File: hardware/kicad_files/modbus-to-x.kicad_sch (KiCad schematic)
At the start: 63 parts, among them J1 PWR, J2 UART, J3 Screw_Terminal_3.5mm_2, J4 SSQ-110-X-X-D, SW1 1825910-7, SW2 1825910-7, U1 AMS1117-3.3, U2 ESP32-WROOM-32DM113DH6400PH3Q0, U3 MAX3485, U5 AT24CS64-XHM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

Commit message: updated datasheets
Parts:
- C22: FriendlyName Cout47uf -> Cin_MAX3485
- J4: PartNo (none) -> SSQ-110-23-L-D
- R1: PartNo RND 1551206S4F1000T5E -> RC1206FR-13120RL
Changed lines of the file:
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@@
 			)
 		)
-		(property "Datasheet" "ESP32-WROOM-32DM113DH6400PH3Q0"
+		(property "Datasheet" "https://www.espressif.com/sites/default/files/documentation/esp32-wroom-32d_esp32-wroom-32u_datasheet_en.pdf"
 			(at 218.948 23.622 0)
 			(effects
@@
 			)
 		)
-		(property "Datasheet" ""
+		(property "Datasheet" "https://docs.rs-online.com/acc8/0900766b8140488f.pdf"
 			(at 245.11 138.43 0)
 			(effects
@@
 			)
 		)
+		(property "PartNo" "SSQ-110-23-L-D"
+			(at 245.11 138.43 90)
+			(effects
+				(font
+					(size 1.27 1.27)
+				)
+				(hide yes)
+			)
+		)
 		(pin "11"
 		)
@@
 			)
 		)
-		(property "FriendlyName" "Cout47uf"
+		(property "FriendlyName" "Cin_MAX3485"
 			(at 36.83 81.28 0)
 			(effects
@@
 			)
 		)
-		(property "Datasheet" "https://media.distrelec.com/Web/Downloads/_t/ds/rnd_smd_resistors_eng_tds.pdf"
+		(property "Datasheet" "https://www.yageo.com/upload/media/product/products/datasheet/rchip/PYu-RC_Group_51_RoHS_L_12.pdf"
 			(at 55.88 99.06 0)
 			(effects
@@
 			)
 		)
-		(property "Description" "Resistor Thick film  100 Ohm     ±1%     SMD 1206 1/4W"
+		(property "Description" "120 Ohms ±1% 0.25W, 1/4W Chip Resistor 1206 (3216 Metric) Moisture Resistant Thick Film"
 			(at 55.88 99.06 0)
 			(effects
@@
 			)
 		)
-		(property "PartNo" "RND 1551206S4F1000T5E"
+		(property "PartNo" "RC1206FR-13120RL"
 			(at 55.88 99.06 90)
 			(effects
 				(font
-					(size 1.27 1.27)
-				)
-				(hide yes)
-			)
-		)
-		(property "ProductCode" ""
-			(at 55.88 99.06 0)
-			(effects
-				(font

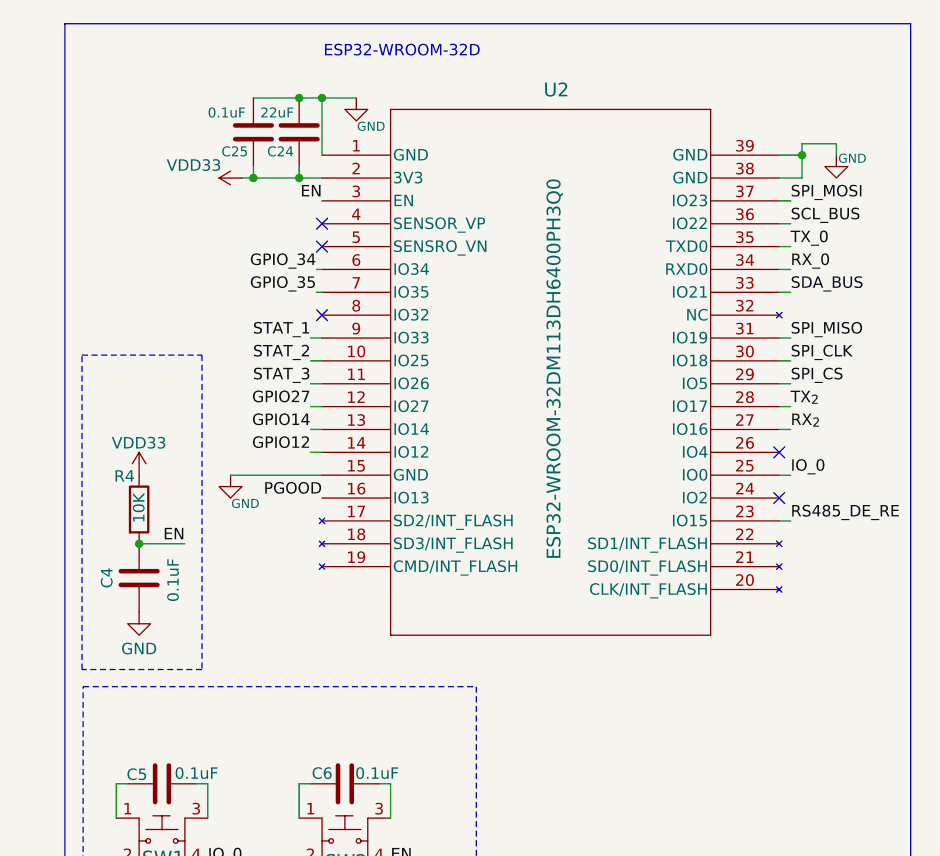
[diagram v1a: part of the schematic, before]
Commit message: fixed esp32 footprint
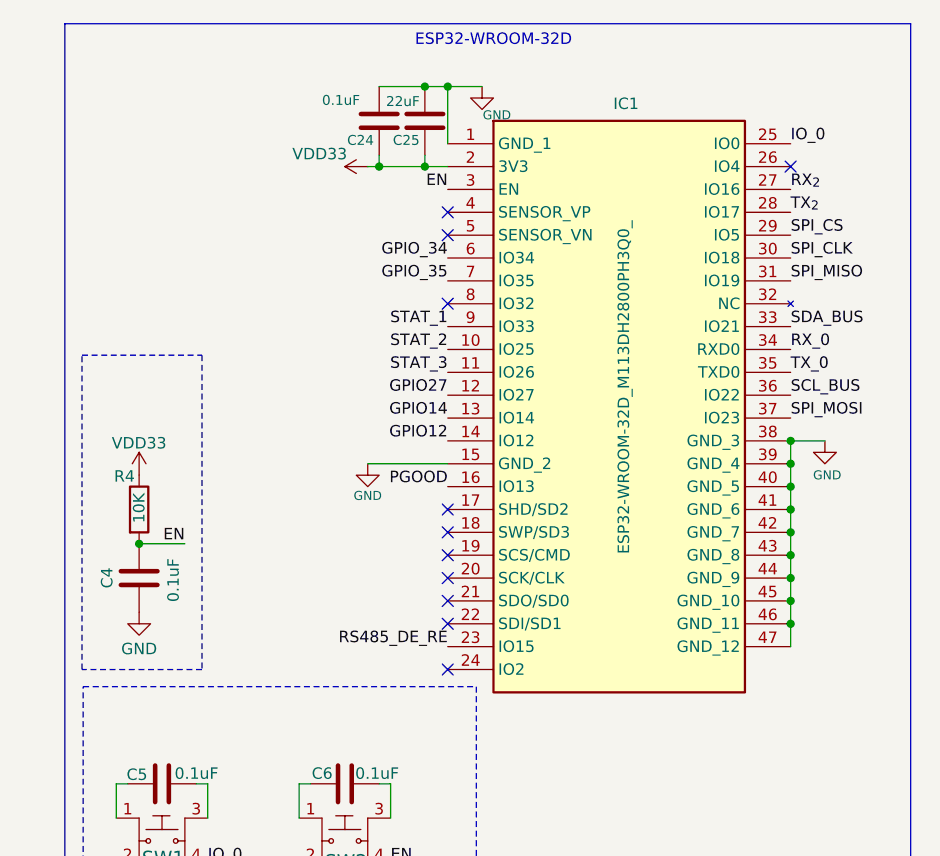
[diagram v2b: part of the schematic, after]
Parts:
- removed U2: ESP32-WROOM-32DM113DH6400PH3Q0, ESP32-WROOM-32D-M113DH6400PH3Q0:ESP32-WROOM-32DM113DH6400PH3Q0_WITH_VIAS, symbol ESP32-WROOM-32D-M113DH6400PH3Q0:ESP32-WROOM-32DM113DH6400PH3Q0
- added IC1: ESP32-WROOM-32D_M113DH2800PH3Q0_, footprint_lib:ESP32-WROOM-32D_M113DH2800PH3Q0, symbol Library:ESP32-WROOM-32D_M113DH2800PH3Q0_
- C24: value 22uF -> 0.1uF; footprint Capacitor_SMD:C_0805_2012Metric_Pad1.18x1.45mm_HandSolder -> Capacitor_SMD:C_1206_3216Metric_Pad1.33x1.80mm_HandSolder; PartNo CL21A226MOCLRNC -> CVNF100K12X; Voltage 16V -> 50V
- C25: value 0.1uF -> 22uF; footprint Capacitor_SMD:C_1206_3216Metric_Pad1.33x1.80mm_HandSolder -> Capacitor_SMD:C_0805_2012Metric_Pad1.18x1.45mm_HandSolder; PartNo CVNF100K12X -> CL21A226MOCLRNC; Voltage 50V -> 16V
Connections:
- net EN: now also IC1.3 (EN)
- net GND: now also IC1.1 (GND_1), IC1.15 (GND_2), IC1.38 (GND_3), IC1.39 (GND_4), IC1.40 (GND_5), IC1.41 (GND_6), IC1.42 (GND_7), IC1.43 (GND_8), IC1.44 (GND_9), IC1.45 (GND_10), IC1.46 (GND_11), IC1.47 (GND_12)
- net GPIO12: now also IC1.14 (IO12)
- net GPIO14: now also IC1.13 (IO14)
- net GPIO27: now also IC1.12 (IO27)
- net GPIO_34: now also IC1.6 (IO34)
- net GPIO_35: now also IC1.7 (IO35)
- net IO_0: now also IC1.25 (IO0)
- net PGOOD: now also IC1.16 (IO13)
- net RS485_DE_RE: now also IC1.23 (IO15)
- net RX_0: now also IC1.34 (RXD0)
- net RX_{2}: now also IC1.27 (IO16)
- net SCL_BUS: now also IC1.36 (IO22)
- net SDA_BUS: now also IC1.33 (IO21)
- net SPI_CLK: now also IC1.30 (IO18)
- net SPI_CS: now also IC1.29 (IO5)
- net SPI_MISO: now also IC1.31 (IO19)
- net SPI_MOSI: now also IC1.37 (IO23)
- net STAT_1: now also IC1.9 (IO33)
- net STAT_2: now also IC1.10 (IO25)
- net STAT_3: now also IC1.11 (IO26)
- net TX_0: now also IC1.35 (TXD0)
- net TX_{2}: now also IC1.28 (IO17)
- net VDD33: now also IC1.2 (3V3)
- no-connect marks 11 -> 17

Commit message: small trace improvements using new ESP footprint
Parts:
- C22: PartNo CHS0001/50 -> NACE1R0M50V4X5.5TR15F
- C23, C24, C4, C5, C6, C9: PartNo CVNF100K12X -> C1206C104K5RACTU
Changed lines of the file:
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@@
 			)
 		)
-		(property "Datasheet" "https://elektronik-lavpris.dk/files/sup2/C1206C104K5RACTU.pdf"
+		(property "Datasheet" "https://content.kemet.com/datasheets/KEM_C1002_X7R_SMD.pdf"
 			(at 224.79 24.13 0)
 			(effects
@@
 			)
 		)
-		(property "Description" "SMD MLC Capacitor 100nF 50V 10% X7R 1206"
+		(property "Description" "0.1 µF ±10% 50V Ceramic Capacitor X7R 1206 (3216 Metric)"
 			(at 224.79 24.13 0)
 			(effects
@@
 			)
 		)
-		(property "PartNo" "CVNF100K12X"
+		(property "PartNo" "C1206C104K5RACTU"
 			(at 224.79 24.13 0)
 			(effects
@@
 			)
 		)
-		(property "Datasheet" "https://elektronik-lavpris.dk/files/sup2/C1206C104K5RACTU.pdf"
+		(property "Datasheet" "https://content.kemet.com/datasheets/KEM_C1002_X7R_SMD.pdf"
 			(at 68.58 138.43 0)
 			(effects
@@
 			)
 		)
-		(property "Description" "SMD MLC Capacitor 100nF 50V 10% X7R 1206"
+		(property "Description" "0.1 µF ±10% 50V Ceramic Capacitor X7R 1206 (3216 Metric)"
 			(at 68.58 138.43 0)
 			(effects
@@
 			)
 		)
-		(property "PartNo" "CVNF100K12X"
+		(property "PartNo" "C1206C104K5RACTU"
 			(at 68.58 138.43 0)
 			(effects
@@
 			)
 		)
-		(property "Datasheet" "https://elektronik-lavpris.dk/files/sup2/C1206C104K5RACTU.pdf"
+		(property "Datasheet" "https://content.kemet.com/datasheets/KEM_C1002_X7R_SMD.pdf"
 			(at 198.12 74.93 0)
 			(effects
@@
 			)
 		)
-		(property "Description" "SMD MLC Capacitor 100nF 50V 10% X7R 1206"
+		(property "Description" "0.1 µF ±10% 50V Ceramic Capacitor X7R 1206 (3216 Metric)"
 			(at 198.12 74.93 0)
 			(effects
@@
 			)
 		)
-		(property "PartNo" "CVNF100K12X"
+		(property "PartNo" "C1206C104K5RACTU"
 			(at 198.12 74.93 0)
 			(effects
@@
 			)
 		)
-		(property "Datasheet" "https://elektronik-lavpris.dk/files/sup2/C1206C104K5RACTU.pdf"
+		(property "Datasheet" "https://content.kemet.com/datasheets/KEM_C1002_X7R_SMD.pdf"
 			(at 26.67 137.16 0)
 			(effects
@@
 			)
 		)
-		(property "Description" "SMD MLC Capacitor 100nF 50V 10% X7R 1206"
+		(property "Description" "0.1 µF ±10% 50V Ceramic Capacitor X7R 1206 (3216 Metric)"
 			(at 26.67 137.16 0)
 			(effects
@@
 			)
 		)
-		(property "PartNo" "CVNF100K12X"
+		(property "PartNo" "C1206C104K5RACTU"
 			(at 26.67 137.16 0)
 			(effects
@@
 			)
 		)
-		(property "Datasheet" "https://elektronik-lavpris.dk/files/sup2/KJ-HT.pdf"
+		(property "Datasheet" "https://www.niccomp.com/wp-content/uploads/catalog/nace.pdf"
 			(at 36.83 81.28 0)
 			(effects
@@
 			)
 		)
-		(property "Description" "SMD El-Capacitor 1uF/50V 4x5,4mm"
+		(property "Description" "1 µF 50 V Aluminum Electrolytic Capacitors Radial, Can - SMD 19.9 Ohm 2000 Hrs @ 85°C"
 			(at 36.83 81.28 0)
 			(effects
@@
 			)
 		)
-		(property "PartNo" "CHS0001/50"
+		(property "PartNo" "NACE1R0M50V4X5.5TR15F"
 			(at 36.83 81.28 0)
 			(effects
@@
 			)
 		)
-		(property "Datasheet" "https://elektronik-lavpris.dk/files/sup2/C1206C104K5RACTU.pdf"
+		(property "Datasheet" "https://content.kemet.com/datasheets/KEM_C1002_X7R_SMD.pdf"
 			(at 220.98 97.79 0)
 			(effects
@@
 			)
 		)
-		(property "Description" "SMD MLC Capacitor 100nF 50V 10% X7R 1206"
+		(property "Description" "0.1 µF ±10% 50V Ceramic Capacitor X7R 1206 (3216 Metric)"
 			(at 220.98 97.79 0)
 			(effects
@@
 			)
 		)
-		(property "PartNo" "CVNF100K12X"
+		(property "PartNo" "C1206C104K5RACTU"
 			(at 220.98 97.79 0)
 			(effects
@@
 			)
 		)
-		(property "Datasheet" "https://elektronik-lavpris.dk/files/sup2/C1206C104K5RACTU.pdf"
+		(property "Datasheet" "https://content.kemet.com/datasheets/KEM_C1002_X7R_SMD.pdf"
 			(at 200.66 97.79 0)
 			(effects
@@
 			)
 		)
-		(property "Description" "SMD MLC Capacitor 100nF 50V 10% X7R 1206"
+		(property "Description" "0.1 µF ±10% 50V Ceramic Capacitor X7R 1206 (3216 Metric)"
 			(at 200.66 97.79 0)
 			(effects
@@
 			)
 		)
-		(property "PartNo" "CVNF100K12X"
+		(property "PartNo" "C1206C104K5RACTU"
 			(at 200.66 97.79 0)
 			(effects

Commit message: added missing component 3dmodels
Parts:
- C1: PartNo CSMK047/35 -> EEH-ZA1V470P
- SW1: Category Switches -> (none); DK_Datasheet_Link https://www.te.com/commerce/DocumentDelivery/DDEController?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 -> (none); DK_Detail_Page /product-detail/en/te-connectivity-alcoswitch-switches/1825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 -> (none); Description_1 SWITCH TACTILE SPST-NO 0.05A 24V -> (none); Digi-Key_PN 450-1804-ND -> (none); Family Tactile Switches -> (none); MPN 1825910-7 -> (none); Manufacturer TE Connectivity ALCOSWITCH Switches -> (none); PartNo (none) -> PTS645SK43SMTR92; Status Active -> (none)
- SW2: Category Switches -> (none); DK_Datasheet_Link https://www.te.com/commerce/DocumentDelivery/DDEController?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 -> (none); DK_Detail_Page /product-detail/en/te-connectivity-alcoswitch-switches/1825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 -> (none); Description_1 SWITCH TACTILE SPST-NO 0.05A 24V -> (none); Digi-Key_PN 450-1804-ND -> (none); Family Tactile Switches -> (none); MPN 1825910-7 -> (none); Manufacturer TE Connectivity ALCOSWITCH Switches -> (none); PartNo (none) -> PTS645SK43SMTR92 LFS; Status Active -> (none)
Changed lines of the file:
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@@
 			)
 		)
-		(property "Datasheet" "https://www.te.com/commerce/DocumentDelivery/DDEController?Action=srchrtrv&DocNm=1825910&DocType=Customer+Drawing&DocLang=English"
+		(property "Datasheet" "https://www.ckswitches.com/media/1471/pts645.pdf"
 			(at 205.74 96.52 0)
 			(effects
@@
 			)
 		)
-		(property "Description" "SWITCH TACTILE SPST-NO 0.05A 24V"
+		(property "Description" "Tactile Switch SPST-NO Top Actuated Surface Mount"
 			(at 200.66 104.14 0)
 			(effects
@@
 			)
 		)
-		(property "Digi-Key_PN" "450-1804-ND"
-			(at 205.74 93.98 0)
-			(effects
-				(font
-					(size 1.524 1.524)
-				)
-				(justify left)
-				(hide yes)
-			)
-		)
-		(property "MPN" "1825910-7"
-			(at 205.74 91.44 0)
-			(effects
-				(font
-					(size 1.524 1.524)
-				)
-				(justify left)
-				(hide yes)
-			)
-		)
-		(property "Category" "Switches"
-			(at 205.74 88.9 0)
-			(effects
-				(font
-					(size 1.524 1.524)
-				)
-				(justify left)
-				(hide yes)
-			)
-		)
-		(property "Family" "Tactile Switches"
-			(at 205.74 86.36 0)
-			(effects
-				(font
-					(size 1.524 1.524)
-				)
-				(justify left)
-				(hide yes)
-			)
-		)
-		(property "DK_Datasheet_Link" "https://www.te.com/commerce/DocumentDelivery/DDEController?Action=srchrtrv&DocNm=1825910&DocType=Customer+Drawing&DocLang=English"
-			(at 205.74 83.82 0)
-			(effects
-				(font
-					(size 1.524 1.524)
-				)
-				(justify left)
-				(hide yes)
-			)
-		)
-		(property "DK_Detail_Page" "/product-detail/en/te-connectivity-alcoswitch-switches/1825910-7/450-1804-ND/1731414"
-			(at 205.74 81.28 0)
-			(effects
-				(font
-					(size 1.524 1.524)
-				)
-				(justify left)
-				(hide yes)
-			)
-		)
-		(property "Description_1" "SWITCH TACTILE SPST-NO 0.05A 24V"
-			(at 205.74 78.74 0)
-			(effects
-				(font
-					(size 1.524 1.524)
-				)
-				(justify left)
-				(hide yes)
-			)
-		)
-		(property "Manufacturer" "TE Connectivity ALCOSWITCH Switches"
-			(at 205.74 76.2 0)
-			(effects
-				(font
-					(size 1.524 1.524)
-				)
-				(justify left)
-				(hide yes)
-			)
-		)
-		(property "Status" "Active"
-			(at 205.74 73.66 0)
+		(property "PartNo" "PTS645SK43SMTR92"
+			(at 200.66 104.14 0)
 			(effects
 				(font
-					(size 1.524 1.524)
+					(size 1.27 1.27)
 				)
-				(justify left)
 				(hide yes)
 			)
@@
 			)
 		)
-		(property "Datasheet" "LMR14020SQDPRTQ1"
+		(property "Datasheet" "LMR14020QDPRRQ1"
 			(at 76.2 40.64 0)
 			(effects
@@
 			)
 		)
-		(property "Description" "SIMPLE SWITCHER® Power Converter 40V 2A, 2.2MHz Step-Down Converter With 40µA IQ"
+		(property "Description" "Buck Switching Regulator IC Positive Adjustable 0.8V 1 Output 2A 10-WDFN Exposed Pad"
 			(at 76.2 40.64 0)
 			(effects
@@
 			)
 		)
-		(property "Datasheet" "https://elektronik-lavpris.dk/files/sup2/CSM.pdf"
+		(property "Datasheet" "https://industrial.panasonic.com/cdbs/www-data/pdf/RDD0000/ABA0000C1221.pdf"
 			(at 31.75 31.75 0)
 			(effects
@@
 			)
 		)
-		(property "Description" "SMD El-Capacitor 47uF/35V 6,3x5,4mm"
+		(property "Description" "47 µF 35 V Aluminum - Polymer Capacitors Radial, Can - SMD 60mOhm 10000 Hrs @ 105°C"
 			(at 31.75 31.75 0)
 			(effects
@@
 			)
 		)
-		(property "PartNo" "CSMK047/35"
+		(property "PartNo" "EEH-ZA1V470P"
 			(at 31.75 31.75 0)
 			(effects
@@
 			)
 		)
-		(property "Datasheet" "https://www.te.com/commerce/DocumentDelivery/DDEController?Action=srchrtrv&DocNm=1825910&DocType=Customer+Drawing&DocLang=English"
+		(property "Datasheet" "https://www.ckswitches.com/media/1471/pts645.pdf"
 			(at 226.06 96.52 0)
 			(effects
@@
 			)
 		)
-		(property "Description" "SWITCH TACTILE SPST-NO 0.05A 24V"
+		(property "Description" "Tactile Switch SPST-NO Top Actuated Surface Mount"
 			(at 220.98 104.14 0)
 			(effects
@@
 			)
 		)
-		(property "Digi-Key_PN" "450-1804-ND"
-			(at 226.06 93.98 0)
-			(effects
-				(font
-					(size 1.524 1.524)
-				)
-				(justify left)
-				(hide yes)
-			)
-		)
-		(property "MPN" "1825910-7"
-			(at 226.06 91.44 0)
-			(effects
-				(font
-					(size 1.524 1.524)
-				)
-				(justify left)
-				(hide yes)
-			)
-		)
-		(property "Category" "Switches"
-			(at 226.06 88.9 0)
-			(effects
-				(font
-					(size 1.524 1.524)
-				)
-				(justify left)
-				(hide yes)
-			)
-		)
-		(property "Family" "Tactile Switches"
-			(at 226.06 86.36 0)
-			(effects
-				(font
-					(size 1.524 1.524)
-				)
-				(justify left)
-				(hide yes)
-			)
-		)
-		(property "DK_Datasheet_Link" "https://www.te.com/commerce/DocumentDelivery/DDEController?Action=srchrtrv&DocNm=1825910&DocType=Customer+Drawing&DocLang=English"
-			(at 226.06 83.82 0)
-			(effects
-				(font
-					(size 1.524 1.524)
-				)
-				(justify left)
-				(hide yes)
-			)
-		)
-		(property "DK_Detail_Page" "/product-detail/en/te-connectivity-alcoswitch-switches/1825910-7/450-1804-ND/1731414"
-			(at 226.06 81.28 0)
-			(effects
-				(font
-					(size 1.524 1.524)
-				)
-				(justify left)
-				(hide yes)
-			)
-		)
-		(property "Description_1" "SWITCH TACTILE SPST-NO 0.05A 24V"
-			(at 226.06 78.74 0)
-			(effects
-				(font
-					(size 1.524 1.524)
-				)
-				(justify left)
-				(hide yes)
-			)
-		)
-		(property "Manufacturer" "TE Connectivity ALCOSWITCH Switches"
-			(at 226.06 76.2 0)
-			(effects
-				(font
-					(size 1.524 1.524)
-				)
-				(justify left)
-				(hide yes)
-			)
-		)
-		(property "Status" "Active"
-			(at 226.06 73.66 0)
+		(property "PartNo" "PTS645SK43SMTR92 LFS"
+			(at 220.98 104.14 0)
 			(effects
 				(font
-					(size 1.524 1.524)
+					(size 1.27 1.27)
 				)
-				(justify left)
 				(hide yes)
 			)

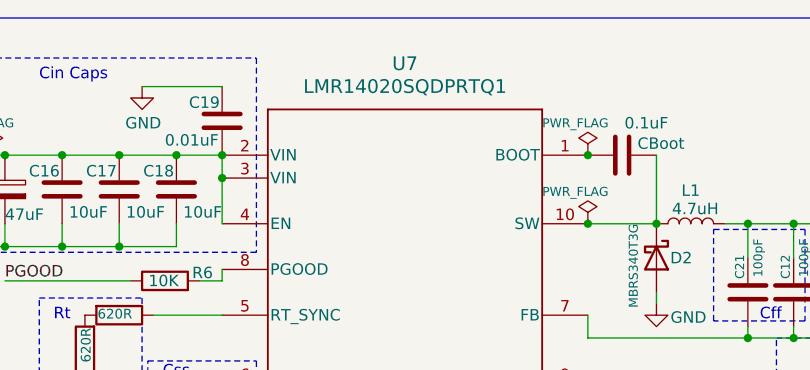
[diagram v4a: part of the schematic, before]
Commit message: added custom footprints to project to avoid warnings
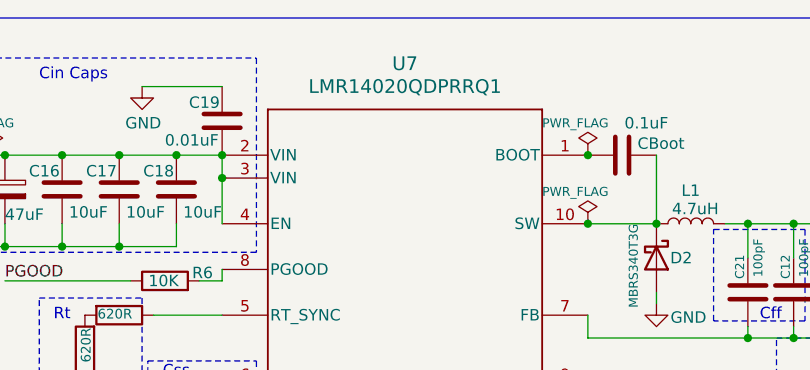
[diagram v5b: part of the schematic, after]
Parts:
- SW1, SW2: footprint digikey-footprints:Switch_Tactile_SMD_6x6mm_PTS645 -> project_footprints:Switch_Tactile_SMD_6x6mm_PTS645_Modified_Silkscreen
- U7: value LMR14020SQDPRTQ1 -> LMR14020QDPRRQ1; footprint LMR14020SQDPRTQ1:DPR0010A_3mm_thermals -> footprint_lib:LMR14020QDPRRQ1_DPR0010A_Modified_3mm_thermals; symbol LMR14020SQDPRTQ1:LMR14020SQDPRTQ1 -> LMR14020QDPRRQ1:LMR14020QDPRRQ1; PartNo LMR14020Q -> LMR14020QDPRRQ1
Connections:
- net GND: no longer U7.V (GND_STITCH)
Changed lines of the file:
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@@
 			)
 		)
-		(property "Footprint" "digikey-footprints:Switch_Tactile_SMD_6x6mm_PTS645"
+		(property "Footprint" "project_footprints:Switch_Tactile_SMD_6x6mm_PTS645_Modified_Silkscreen"
 			(at 205.74 99.06 0)
 			(effects
@@
 	)
 	(symbol
-		(lib_id "LMR14020SQDPRTQ1:LMR14020SQDPRTQ1")
+		(lib_id "LMR14020QDPRRQ1:LMR14020QDPRRQ1")
 		(at 76.2 40.64 0)
 		(unit 1)
@@
 			)
 		)
-		(property "Value" "LMR14020SQDPRTQ1"
+		(property "Value" "LMR14020QDPRRQ1"
 			(at 76.2 20.32 0)
 			(effects
@@
 			)
 		)
-		(property "Footprint" "LMR14020SQDPRTQ1:DPR0010A_3mm_thermals"
+		(property "Footprint" "footprint_lib:LMR14020QDPRRQ1_DPR0010A_Modified_3mm_thermals"
 			(at 76.2 40.64 0)
 			(effects
@@
 			)
 		)
-		(property "Datasheet" "LMR14020QDPRRQ1"
+		(property "Datasheet" "https://www.ti.com/lit/gpn/lmr14020-q1"
 			(at 76.2 40.64 0)
 			(effects
@@
 			)
 		)
-		(property "PartNo" "LMR14020Q"
+		(property "PartNo" "LMR14020QDPRRQ1"
 			(at 76.2 40.64 0)
 			(effects
@@
 		(pin "7"
 		)
-		(pin "V"
-		)
 		(instances
 			(project ""
@@
 			)
 		)
-		(property "Footprint" "digikey-footprints:Switch_Tactile_SMD_6x6mm_PTS645"
+		(property "Footprint" "project_footprints:Switch_Tactile_SMD_6x6mm_PTS645_Modified_Silkscreen"
 			(at 226.06 99.06 0)
 			(effects
